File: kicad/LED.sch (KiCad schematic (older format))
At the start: 32 parts, among them P4 LED_OUT

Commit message: added kicad PCB wip
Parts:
- added C11, C12, C13, C14, C15, C16: C_NPOL, symbol halo:C_NPOL
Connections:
- wire segments 172 -> 202
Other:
- moved on the sheet: B20

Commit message: added qwiic I2C conn for ToF sensor
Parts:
- C11, C12, C13, C14, C15, C16: footprint (none) -> halo:C_0805_2012Metric
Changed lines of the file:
@@
 F 0 "C11" H 5578 1896 50  0000 L CNN
 F 1 "C_NPOL" H 5578 1805 50  0000 L CNN
-F 2 "" H 5450 1875 60  0000 C CNN
+F 2 "halo:C_0805_2012Metric" H 5450 1875 60  0001 C CNN
 F 3 "" H 5450 1875 60  0000 C CNN
 	1    5450 1850
@@
 F 0 "C12" H 9578 1896 50  0000 L CNN
 F 1 "C_NPOL" H 9578 1805 50  0000 L CNN
-F 2 "" H 9450 1875 60  0000 C CNN
+F 2 "halo:C_0805_2012Metric" H 9450 1875 60  0001 C CNN
 F 3 "" H 9450 1875 60  0000 C CNN
 	1    9450 1850
@@
 F 0 "C13" H 5553 3896 50  0000 L CNN
 F 1 "C_NPOL" H 5553 3805 50  0000 L CNN
-F 2 "" H 5425 3875 60  0000 C CNN
+F 2 "halo:C_0805_2012Metric" H 5425 3875 60  0001 C CNN
 F 3 "" H 5425 3875 60  0000 C CNN
 	1    5425 3850
@@
 F 0 "C14" H 9553 3896 50  0000 L CNN
 F 1 "C_NPOL" H 9553 3805 50  0000 L CNN
-F 2 "" H 9425 3875 60  0000 C CNN
+F 2 "halo:C_0805_2012Metric" H 9425 3875 60  0001 C CNN
 F 3 "" H 9425 3875 60  0000 C CNN
 	1    9425 3850
@@
 F 0 "C15" H 5503 5921 50  0000 L CNN
 F 1 "C_NPOL" H 5503 5830 50  0000 L CNN
-F 2 "" H 5375 5900 60  0000 C CNN
+F 2 "halo:C_0805_2012Metric" H 5375 5900 60  0001 C CNN
 F 3 "" H 5375 5900 60  0000 C CNN
 	1    5375 5875
@@
 F 0 "C16" H 9503 5921 50  0000 L CNN
 F 1 "C_NPOL" H 9503 5830 50  0000 L CNN
-F 2 "" H 9375 5900 60  0000 C CNN
+F 2 "halo:C_0805_2012Metric" H 9375 5900 60  0001 C CNN
 F 3 "" H 9375 5900 60  0000 C CNN
 	1    9375 5875

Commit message: added PCB review needed
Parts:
- D1, D10, D11, D12, D13, D14, D15, D16, D17, D18, D19, D2, D20, D21, D22, D23, D24, D25, D26, D27, D28, D29, D3, D30, D4, D5, D6, D7, D8, D9: footprint LED_SMD:LED_WS2812B_PLCC4_5.0x5.0mm_P3.2mm -> halo:LED_WS2812B_PLCC4_5.0x5.0mm_P3.2mm; symbol LED:WS2812B -> halo:WS2812B
- P4: footprint Connector_PinSocket_2.54mm:PinSocket_1x04_P2.54mm_Vertical_SMD_Pin1Left -> halo:PinSocket_1x04_P2.54mm_Vertical_SMD_Pin1Left

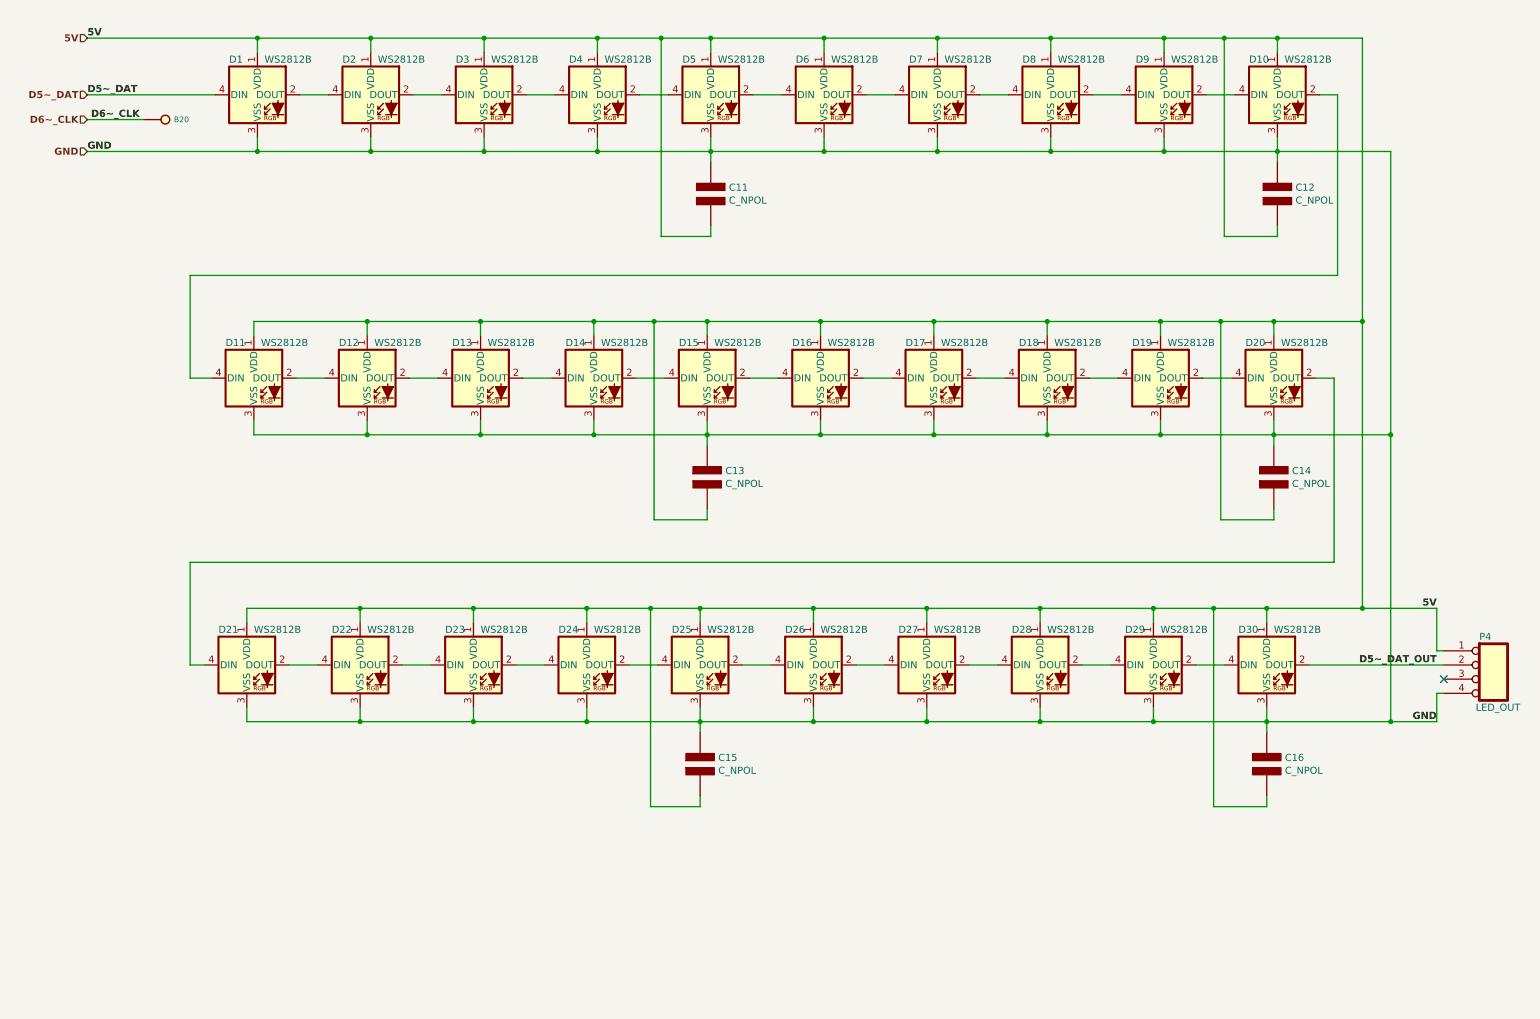
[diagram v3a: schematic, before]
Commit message: Gerber BoM ready
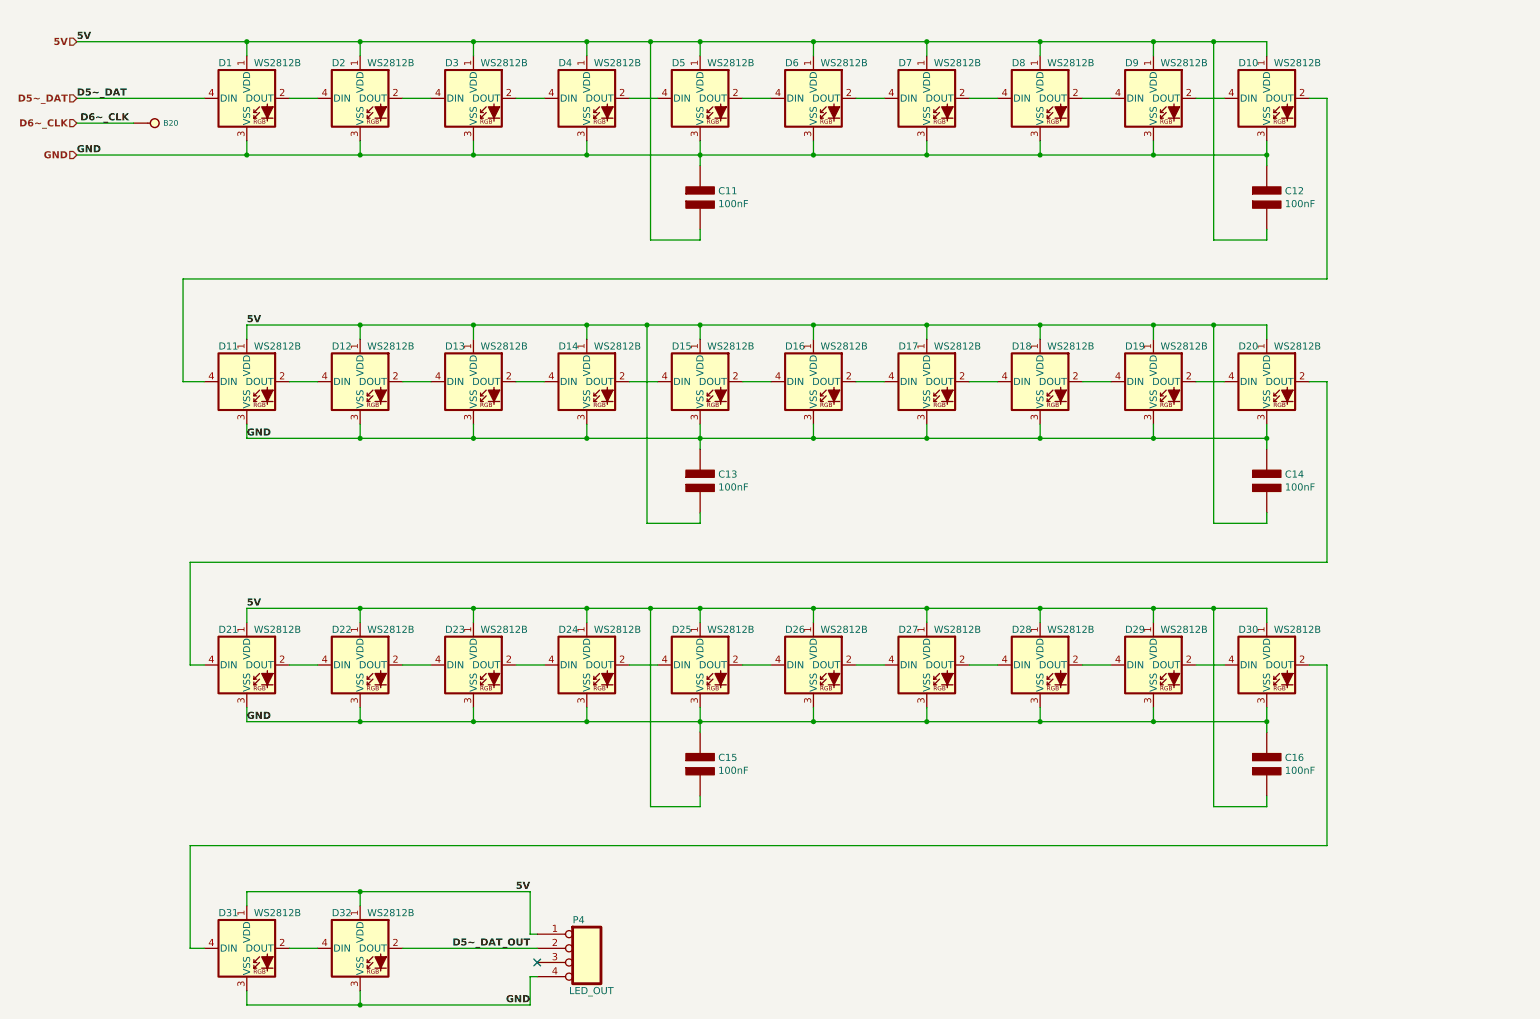
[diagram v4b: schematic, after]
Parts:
- added D31, D32: WS2812B, halo:LED_WS2812B_PLCC4_5.0x5.0mm_P3.2mm, symbol halo:WS2812B
- C11, C12, C13, C14, C15, C16: value C_NPOL -> 100nF
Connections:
- net 5V: now also D31.1 (VDD), D32.1 (VDD)
- net D5~~_DAT_OUT: now also D32.2 (DOUT); no longer D30.2 (DOUT)
- net GND: now also D31.3 (VSS), D32.3 (VSS)
- new net: D31.2 (DOUT), D32.4 (DIN)
- new net: D30.2 (DOUT), D31.4 (DIN)
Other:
- moved on the sheet: B20, C11, C12, C13, C14, D1, D10, D11, D12, D13, D14, D15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

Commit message: Gerber BoM Position files for JLCpcb
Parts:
- added B21: I_O, halo:breakout_smd, symbol halo:I_O
- P4: symbol halo:CONN_4 -> halo:CONN_01x04
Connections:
- net at P4.3 (Pin_3): now also B21.1
- net D5~~_DAT renamed DAT
- net D5~~_DAT_OUT renamed DAT_OUT
- net D6~~_CLK renamed CLK
- no-connect marks 1 -> 0
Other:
- moved on the sheet: P4
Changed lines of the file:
@@
 GND
 Text Label 975  1175 0    50   ~ 10
-D5~~_DAT
+DAT
 Text Label 4175 7175 2    50   ~ 10
-D5~~_DAT_OUT
+DAT_OUT
 Text Label 4175 6775 2    50   ~ 10
 5V
@@
 5V
 Text HLabel 975  1175 0    50   Input ~ 10
-D5~~_DAT
+DAT
 Text HLabel 975  1575 0    50   Input ~ 10
 GND
 Text HLabel 975  1350 0    50   Input ~ 10
-D6~~_CLK
+CLK
 Wire Wire Line
 	975  1350 1375 1350
 Text Label 1000 1350 0    50   ~ 10
-D6~~_CLK
+CLK
 $Comp
 L halo:I_O B20
@@
 $EndComp
 $Comp
-L halo:CONN_4 P4
+L halo:CONN_01x04 P4
 U 1 1 5FF42D78
-P 4575 7225
-F 0 "P4" H 4475 7475 50  0000 L CNN
-F 1 "LED_OUT" H 4450 6975 50  0000 L CNN
-F 2 "halo:PinSocket_1x04_P2.54mm_Vertical_SMD_Pin1Left" H 4575 7225 60  0001 C CNN
-F 3 "" H 4575 7225 60  0000 C CNN
-	1    4575 7225
+P 4475 7225
+F 0 "P4" H 4375 7475 50  0000 L CNN
+F 1 "LED_OUT" V 4550 7075 50  0000 L CNB
+F 2 "halo:PinSocket_1x04_P2.54mm_Vertical_SMD_Pin1Left" H 4475 7225 60  0001 C CNN
+F 3 "" H 4475 7225 60  0000 C CNN
+	1    4475 7225
 	1    0    0    -1
 $EndComp
@@
 Wire Wire Line
 	4175 7375 4175 7575
-NoConn ~ 4225 7275
 $Comp
 L halo:C_NPOL C11
@@
 Text Label 2175 5575 0    50   ~ 10
 GND
+$Comp
+L halo:I_O B21
+U 1 1 605C58B0
+P 4000 7275
+F 0 "B21" H 4060 7275 40  0000 L CNN
+F 1 "I_O" H 4000 7330 30  0001 C CNN
+F 2 "halo:breakout_smd" H 4000 7275 60  0001 C CNN
+F 3 "" H 4000 7275 60  0000 C CNN
+	1    4000 7275
+	-1   0    0    1
+$EndComp
+Wire Wire Line
+	4225 7275 4150 7275
 $EndSCHEMATC
